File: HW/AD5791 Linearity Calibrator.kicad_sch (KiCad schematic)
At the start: 47 parts, among them J1 OUTPUT, J2 PWR, U1 Pico, U10 OPA189, U11 7533, U2 AD5791BRUZ, U3 LT1013, U4 OPA189, U5 OPA189, U6 OPA189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

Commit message: Layout 1
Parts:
- removed H1, H4: MountingHole, MountingHole:MountingHole_3.2mm_M3_Pad_Via, symbol Mechanical:MountingHole
- added NT1: MECCA, Connector_PinHeader_1.27mm:PinHeader_1x02_P1.27mm_Vertical, symbol Device:NetTie_2
- JP1: footprint (none) -> Jumper:SolderJumper-2_P1.3mm_Bridged2Bar_RoundedPad1.0x1.5mm
- R2: footprint Resistor_SMD:R_0603_1608Metric -> Resistor_SMD:R_1206_3216Metric
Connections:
- net GND: now also NT1.2; no longer U10.3 (+), U2.19 (AGND), U3.5 (+), U7.1 (-REFS), U7.2 (-REFF)
- net SCLK: now also U1.4 (GPIO2)
- net SDIN: now also U1.2 (GPIO1)
- net SDO: now also U1.1 (GPIO0)
- net SENSE+: now also RN1.1 (R1.1); no longer RN1.8 (R1.2)
- net SENSE-: now also RN1.2 (R2.1); no longer RN1.7 (R2.2)
- net ~{CLR}: now also U1.7 (GPIO5)
- net ~{LDAC}: now also U1.9 (GPIO6)
- net ~{RESET}: now also U1.6 (GPIO4)
- net ~{SYNC}: now also U1.5 (GPIO3)
- new net: RN1.7 (R2.2), RN1.8 (R1.2), U4.3 (+)
- new net GNDA: NT1.1, U10.3 (+), U2.19 (AGND), U3.5 (+), U7.1 (-REFS), U7.2 (-REFF)
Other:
- moved on the sheet: J1, RN1A, RN1B

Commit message: Finished Layout?
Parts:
- removed H2, H3: MountingHole, MountingHole:MountingHole_3.2mm_M3_Pad_Via, symbol Mechanical:MountingHole
- removed JP1: BYP, Jumper:SolderJumper-2_P1.3mm_Bridged2Bar_RoundedPad1.0x1.5mm, symbol Jumper:SolderJumper_2_Bridged
- removed NT1: MECCA, Connector_PinHeader_1.27mm:PinHeader_1x02_P1.27mm_Vertical, symbol Device:NetTie_2
- added D1: 5819, Diode_SMD:D_SOD-323, symbol Device:D_Small
- added H1, H2, H3, H5: MountingHole_Pad, MountingHole:MountingHole_3.2mm_M3_Pad_Via, symbol Mechanical:MountingHole_Pad
- added J3: TEMP, Connector_PinHeader_2.54mm:PinHeader_1x06_P2.54mm_Vertical, symbol Connector_Generic:Conn_01x06
- added J4: REF, Connector_PinHeader_2.54mm:PinHeader_1x02_P2.54mm_Vertical, symbol Connector_Generic:Conn_01x02
- added SW1: RST, Connector_PinHeader_2.54mm:PinHeader_1x02_P2.54mm_Vertical, symbol Switch:SW_SPST
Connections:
- net GNDA is gone; now on net GND: U10.3 (+), U2.19 (AGND), U3.5 (+), U7.1 (-REFS), U7.2 (-REFF)
- net +15V: now also D1.1 (K)
- net +3.3V: now also C3.1, U1.36 (3V3), U2.10 (IOVCC), U2.9 (VCC), J3.4 (Pin_4)
- net -15V: now also C4.1, U2.18 (VSS)
- net GND: now also H1.1, H2.1, H3.1, H5.1, J3.3 (Pin_3), J4.2 (Pin_2), SW1.1 (A)
- net 7VREF: now reaches R2.2, U3.3 (+), U7.6 (+REFF), U7.7 (+REFS)
- net 7VREF: now also J4.1 (Pin_1)
- net ADD0: now reaches U1.17 (GPIO13)
- net ADD0: now also J3.6 (Pin_6)
- net SDA: now reaches U1.19 (GPIO14)
- net SDA: now also J3.5 (Pin_5)
- net SCL: now reaches U1.20 (GPIO15)
- net SCL: now also J3.2 (Pin_2)
- net ALERT: now reaches U1.21 (GPIO16)
- net ALERT: now also J3.1 (Pin_1)
- net at U1.30 (RUN): now also SW1.2 (B)
- net at U1.39 (VSYS): now also D1.2 (A)
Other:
- note added: "On-board 3V3 reg deactivated"
- moved on the sheet: C4

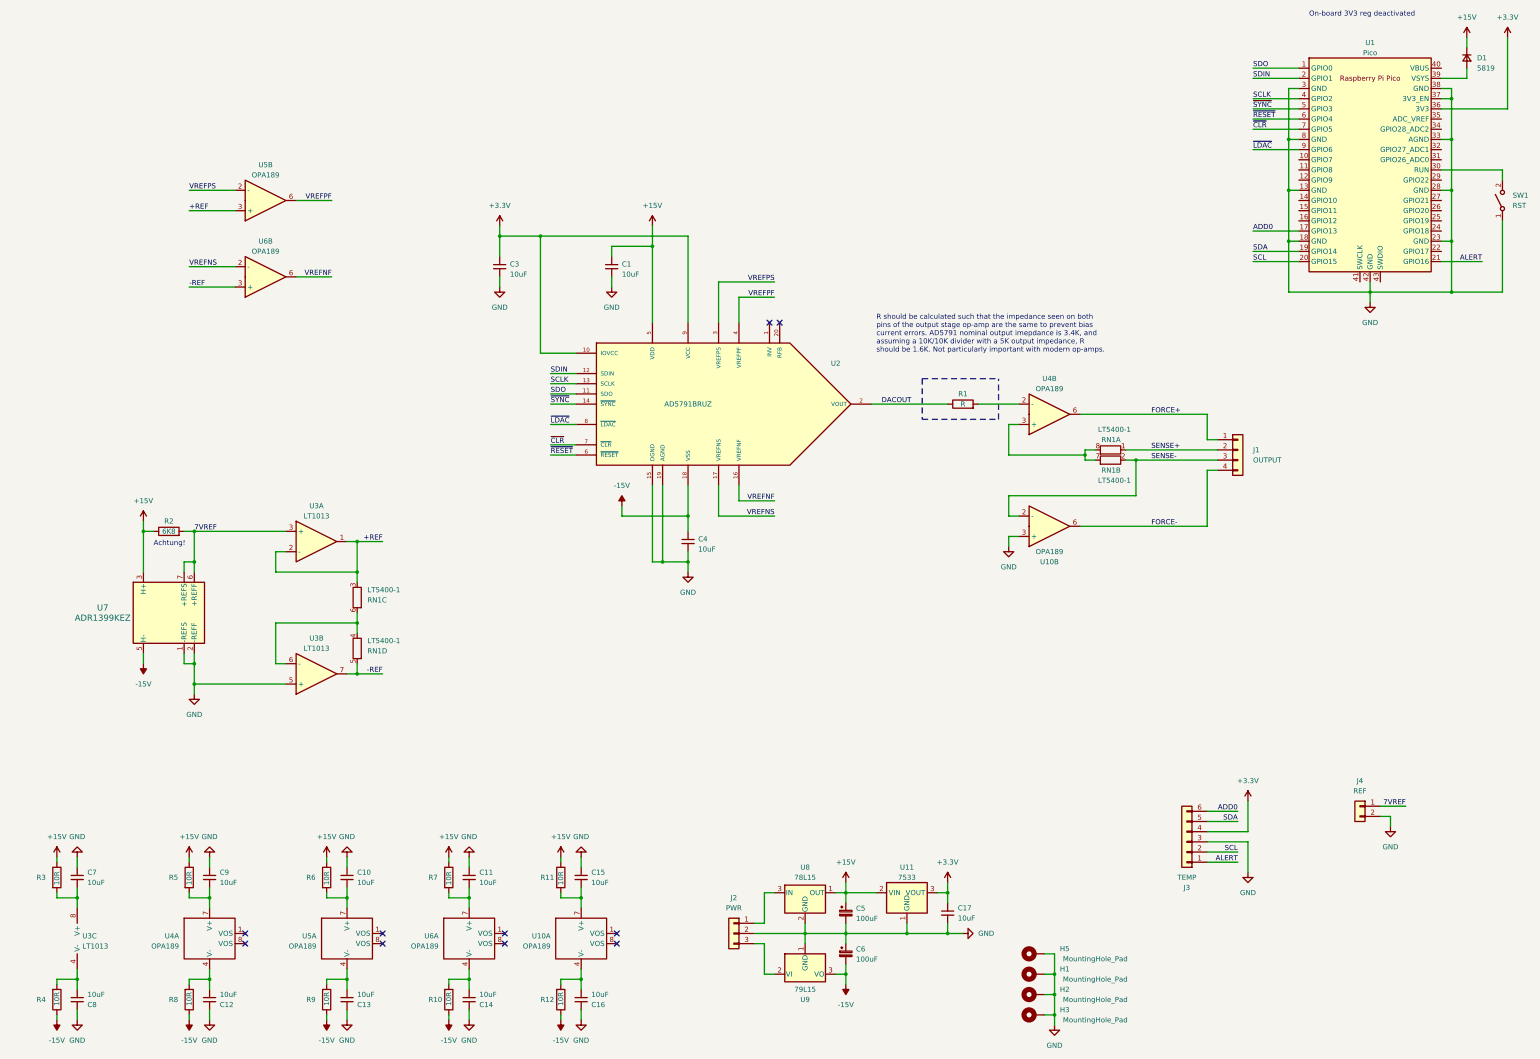
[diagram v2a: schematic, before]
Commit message: Mark's Suggestions 1
- Removed redundant reference buffers and modified reference buffer/scaler
- Added passive compensation components around ADR1399
- Added diode from output of 15V regulator to input of 3.3V regulator to prevent backfeeding when powered by USB
- Removed temperature sensor module from PCB (add breakout headers later?)
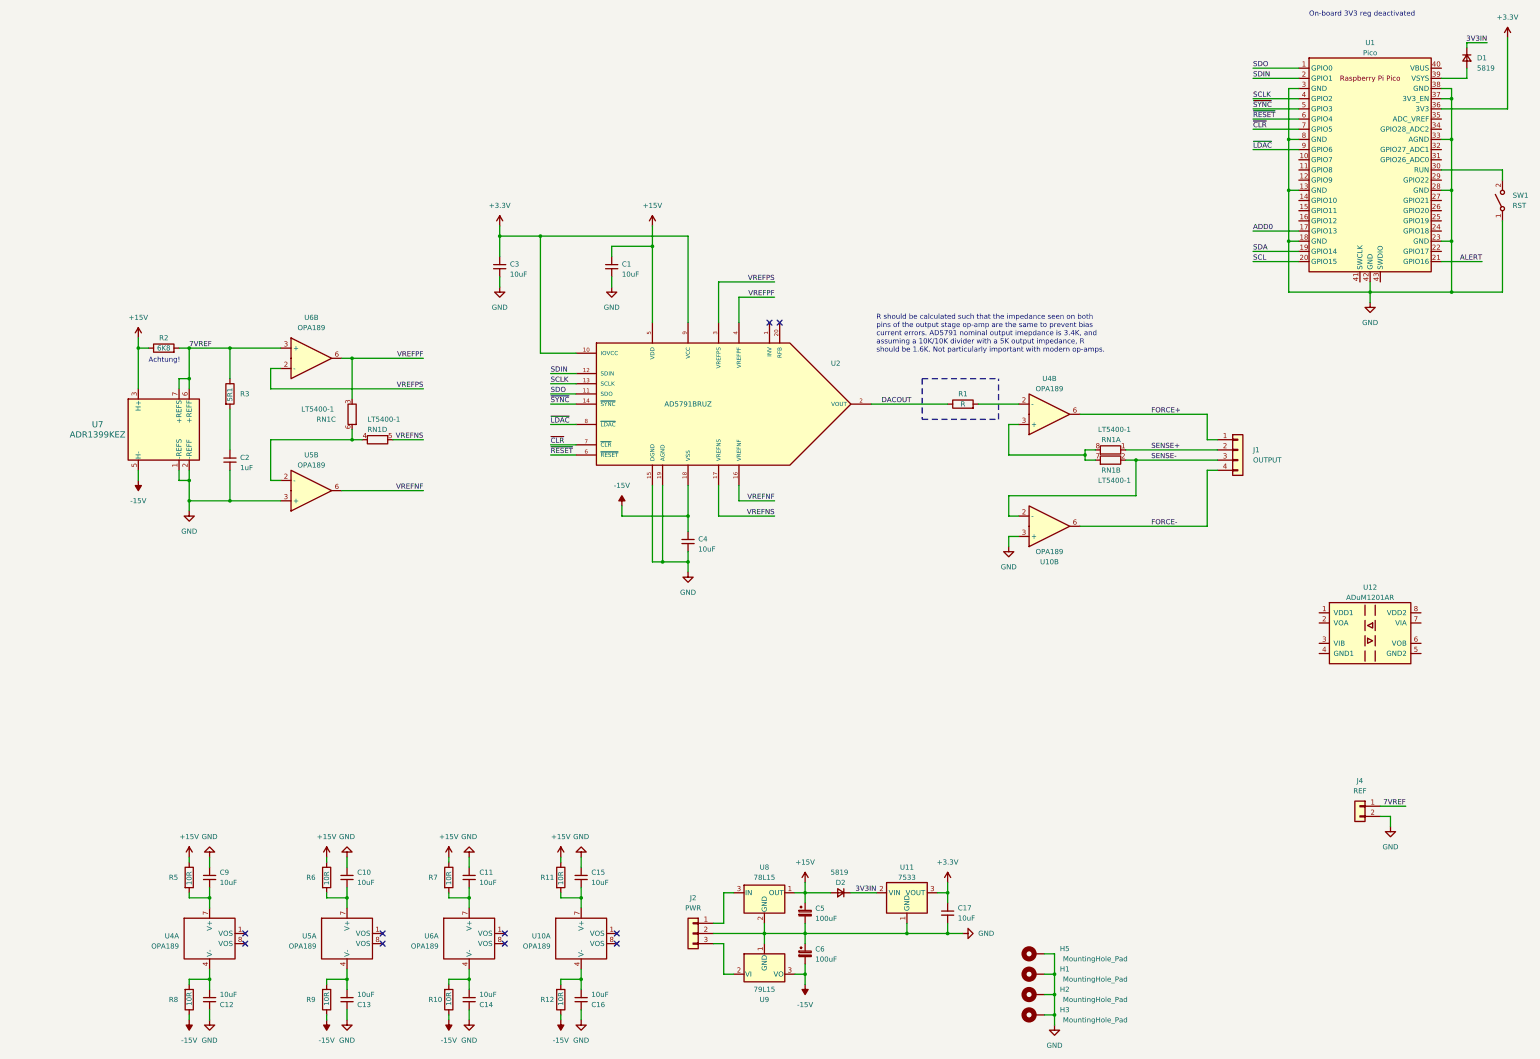
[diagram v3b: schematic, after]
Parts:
- removed C7, C8: 10uF, Resistor_SMD:R_0603_1608Metric, symbol Device:C_Small
- removed J3: TEMP, Connector_PinHeader_2.54mm:PinHeader_1x06_P2.54mm_Vertical, symbol Connector_Generic:Conn_01x06
- removed R4: 10R, Resistor_SMD:R_0603_1608Metric, symbol Device:R
- removed U3: LT1013, Package_SO:SOIC-8_3.9x4.9mm_P1.27mm, symbol Device:Opamp_Dual
- added C2: 1uF, Resistor_SMD:R_0603_1608Metric, symbol Device:C_Small
- added D2: 5819, Diode_SMD:D_SOD-323, symbol Device:D_Small
- added U12: ADuM1201AR, Package_SO:SOIC-8_3.9x4.9mm_P1.27mm, symbol Isolator:ADuM1201AR
- R3: value 10R -> 5R1
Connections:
- net +15V: now also D2.2 (A); no longer D1.1 (K), R3.1, U11.2 (VIN)
- net 7VREF: now also R3.1, U6.3 (+)
- net GND: now also U5.3 (+), C2.2
- net VREFNF: now also U5.6; no longer U6.6
- net VREFNS: now also RN1.5 (R4.2); no longer U6.2 (-)
- net VREFPF: now also RN1.3 (R3.1), U6.6; no longer U5.6
- net VREFPS: now also U6.2 (-); no longer U5.2 (-)
- net at RN1.4 (R4.1), RN1.6 (R3.2): now also U5.2 (-)
- net at R3.2: now also C2.1
- removed net +REF: RN1.3 (R3.1), U5.3 (+)
- removed net -REF: RN1.5 (R4.2), U6.3 (+)
- new net 3V3IN: D1.1 (K), D2.1 (K), U11.2 (VIN)
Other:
- moved on the sheet: C5, C6, J2, R2, RN1C, RN1D, U5B, U6B, U7, U8, U9

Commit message: NOMC network
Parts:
- removed C15, C16: 10uF, Resistor_SMD:R_0603_1608Metric, symbol Device:C_Small
- removed J1: OUTPUT, Connector_PinHeader_2.54mm:PinHeader_1x04_P2.54mm_Vertical, symbol Connector_Generic:Conn_01x04
- removed R11, R12: 10R, Resistor_SMD:R_0603_1608Metric, symbol Device:R
- removed RN1: LT5400-1, Package_SO:MSOP-8-1EP_3x3mm_P0.65mm_EP1.68x1.88mm, symbol Device:R_Pack04_Split
- removed U10: OPA189, Package_SO:SOIC-8_3.9x4.9mm_P1.27mm, symbol Better Op-Amp:Better_Op-Amp
- added D3, D4: 5819, Diode_SMD:D_SOD-323, symbol Device:D_Small
- added J1: OUTPUT, Connector_PinHeader_2.54mm:PinHeader_1x02_P2.54mm_Vertical, symbol Connector_Generic:Conn_01x02
- added R4: 100K, Resistor_SMD:R_0603_1608Metric, symbol Device:R
- added RN1: 10K, Package_SO:SOIC-16_3.9x9.9mm_P1.27mm, symbol Device:R_Pack08_Split
- D2: footprint Diode_SMD:D_SOD-323 -> Diode_SMD:D_SOD-123
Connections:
- net FORCE+ is gone; now on an unnamed net: U4.6
- net +15V: now also R4.1; no longer R2.1
- net 7VREF: now also R2.1, R4.2; no longer R2.2
- net GND: now also J1.2 (Pin_2)
- net VREFNF: now also D4.2 (A); no longer U5.6
- net VREFNS: now also RN1.5 (R5.1), RN1.6 (R6.1)
- net VREFPF: now also R2.2, D3.1 (K); no longer U6.6
- net VREFPS: now also RN1.15 (R2.2), RN1.16 (R1.2); no longer U6.2 (-)
- net at U4.3 (+): now also J1.1 (Pin_1)
- net at U5.2 (-): now also RN1.13 (R4.2), RN1.3 (R3.1)
- new net: RN1.11 (R6.2), RN1.12 (R5.2), RN1.4 (R4.1)
- new net: RN1.1 (R1.1), RN1.14 (R3.2), RN1.2 (R2.1), U6.2 (-)
- new net: D3.2 (A), U6.6
- new net: D4.1 (K), U5.6
- no-connect marks 10 -> 8
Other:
- moved on the sheet: C1, C10, C11, C12, C13, C14, C17, C2, C3, C4, C5, C6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

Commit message: total creative block
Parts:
- D1: footprint Diode_SMD:D_SOD-323 -> Diode_SMD:D_SOD-123
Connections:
- net SCLK: no longer U1.4 (GPIO2)
- net SDIN: no longer U1.2 (GPIO1)
- net SDO: no longer U1.1 (GPIO0)
- net VREFNS: now also RN1.14 (R3.2), RN1.15 (R2.2); no longer RN1.5 (R5.1), RN1.6 (R6.1)
- net VREFPS: now also RN1.10 (R7.2), RN1.9 (R8.2); no longer RN1.15 (R2.2), RN1.16 (R1.2)
- net ~{CLR}: no longer U1.7 (GPIO5)
- net ~{LDAC}: no longer U1.9 (GPIO6)
- net ~{RESET}: no longer U1.6 (GPIO4)
- net ~{SYNC}: no longer U1.5 (GPIO3)
- net at U4.2 (-): now also J1.1 (Pin_1), U4.6; no longer R1.2
- net at RN1.7 (R7.1): now also RN1.11 (R6.2), RN1.8 (R8.1), U6.2 (-)
- new net: RN1.1 (R1.1), RN1.6 (R6.1), U5.2 (-)
- new net: R1.2, U4.3 (+)
- new net: RN1.16 (R1.2), RN1.2 (R2.1), RN1.3 (R3.1)
- now unconnected: RN1.12 (R5.2), RN1.13 (R4.2), RN1.4 (R4.1)
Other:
- moved on the sheet: RN1A, RN1B, RN1C, RN1D, RN1E, RN1F, RN1G, RN1H

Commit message: Backup commit
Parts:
- removed C17: 10uF, Resistor_SMD:R_0603_1608Metric, symbol Device:C_Small
- removed D4: 5819, Diode_SMD:D_SOD-323, symbol Device:D_Small
- removed U7: ADR1399KEZ, ADR1399KEZ:LCC8_E-8-2_ADI, symbol ADR1399KEZ:ADR1399KEZ
- added C15: 10uF, Resistor_SMD:R_0603_1608Metric, symbol Device:C_Small
- added C16: 1uF, Resistor_SMD:R_0603_1608Metric, symbol Device:C_Small
- added C7: 100uF, Capacitor_SMD:CP_Elec_6.3x5.4, symbol Device:C_Polarized_Small
- added C8: 10nF, Resistor_SMD:R_0603_1608Metric, symbol Device:C_Small
- added R11: 10K, Resistor_SMD:R_0603_1608Metric, symbol Device:R
- added U3: LM399, Package_TO_SOT_THT:Analog_TO-46-4_ThermalShield, symbol Reference_Voltage:LM399
- D1, D2: footprint Diode_SMD:D_SOD-123 -> Resistor_SMD:R_0603_1608Metric_Pad0.98x0.95mm_HandSolder
- D3: footprint Diode_SMD:D_SOD-323 -> Resistor_SMD:R_0603_1608Metric_Pad0.98x0.95mm_HandSolder
- R2: footprint Resistor_SMD:R_1206_3216Metric -> Resistor_SMD:R_0603_1608Metric
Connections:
- net +15V: now also C16.1, U3.3
- net +3.3V: now also U12.8 (VDD2), C15.1, C7.1
- net -15V: now also C16.2, U3.4
- net 7VREF: now also C8.1, R11.2; no longer R2.1, R3.1, R4.2
- net GND: now also U12.5 (GND2), C15.2, C7.2, C8.2, U3.2
- net SCLK: now also U1.9 (GPIO6)
- net SDIN: now also U1.7 (GPIO5)
- net SDO: now also U1.6 (GPIO4)
- net VREFNF: now also U5.6
- net VREFPF: now also D3.2 (A), U6.6; no longer D3.1 (K), R2.2
- net ~{CLR}: now also U1.12 (GPIO9)
- net ~{LDAC}: now also U1.14 (GPIO10)
- net ~{RESET}: now also U1.11 (GPIO8)
- net ~{SYNC}: now also U1.10 (GPIO7)
- new net: D3.1 (K), R2.2
- new net REF: R11.1, R2.1, R3.1, R4.2, U3.1
- no-connect marks 8 -> 12
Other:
- moved on the sheet: D3, RN1E, U12, U5B, U6B

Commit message: Layout Revision 2
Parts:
- added J3, J5, J6: REF, Connector_PinHeader_2.54mm:PinHeader_1x02_P2.54mm_Vertical, symbol Connector_Generic:Conn_01x02
- SW1: footprint Connector_PinHeader_2.54mm:PinHeader_1x02_P2.54mm_Vertical -> Button_Switch_SMD:SW_SPST_B3U-1000P
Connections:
- net +15V: now also J3.1 (Pin_1)
- net +3.3V: now also J6.1 (Pin_1)
- net -15V: now also J5.1 (Pin_1)
- net 7VREF: no longer J4.1 (Pin_1)
- net GND: now also J3.2 (Pin_2), J5.2 (Pin_2), J6.2 (Pin_2)
- net REF: now also J4.1 (Pin_1)
- net SCLK: now also U1.7 (GPIO5); no longer U1.9 (GPIO6)
- net SDIN: now also U1.6 (GPIO4); no longer U1.7 (GPIO5)
- net SDO: now also U1.5 (GPIO3); no longer U1.6 (GPIO4)
- net ~{CLR}: now also U1.11 (GPIO8); no longer U1.12 (GPIO9)
- net ~{LDAC}: now also U1.12 (GPIO9); no longer U1.14 (GPIO10)
- net ~{RESET}: now also U1.10 (GPIO7); no longer U1.11 (GPIO8)
- net ~{SYNC}: now also U1.9 (GPIO6); no longer U1.10 (GPIO7)
